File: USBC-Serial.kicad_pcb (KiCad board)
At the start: 2 copper layers, 19.5 x 25.9 mm, 10 parts, among them J1 USB_C_Receptacle_USB2.0_16P, J2 Conn_01x06_Pin, U1 CH343P

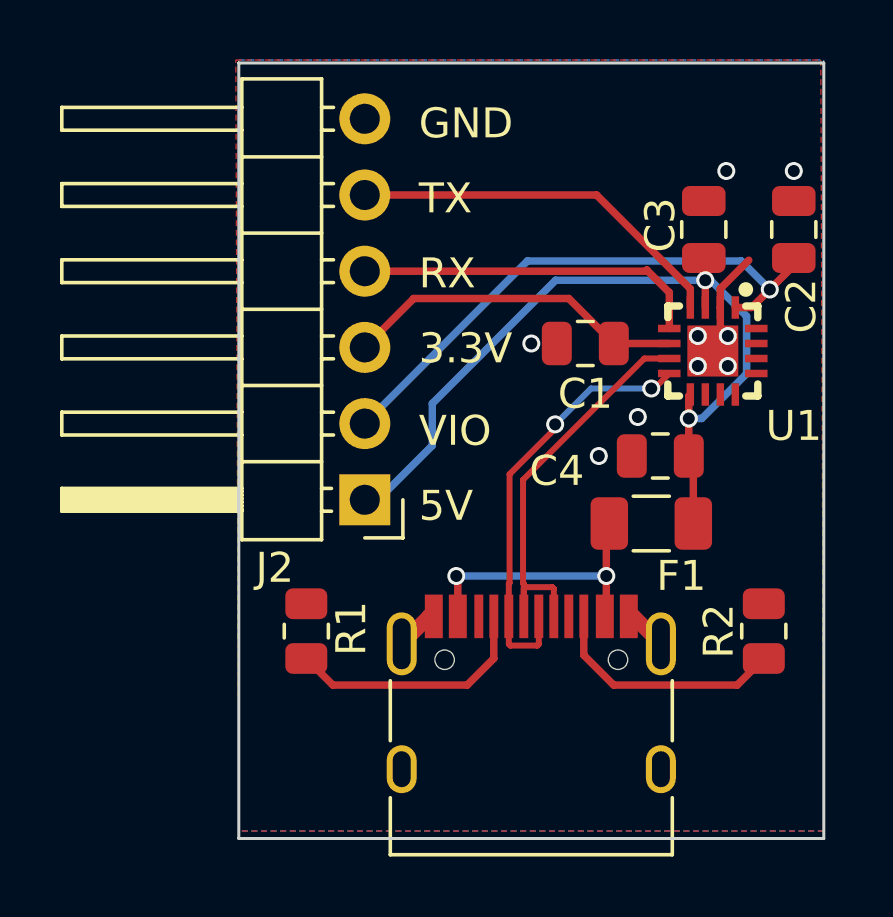
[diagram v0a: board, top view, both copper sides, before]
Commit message: fix bypass caps
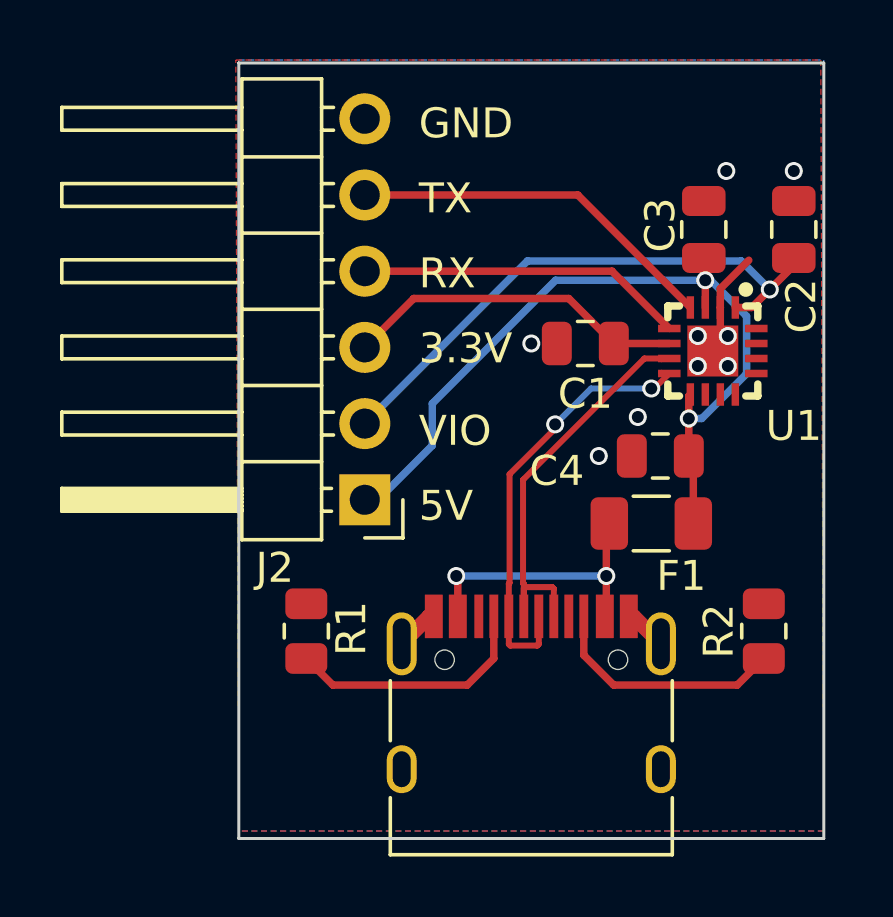
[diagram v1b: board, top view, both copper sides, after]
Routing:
- net /RXD: track 11.7 -> 10.9 mm
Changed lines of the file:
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@@
   (segment (start 25.495051 37.135483) (end 24.5 36.140432) (width 0.25) (layer "F.Cu") (net 10))
   (segment (start 29.614517 37.135483) (end 25.495051 37.135483) (width 0.25) (layer "F.Cu") (net 10))
-  (segment (start 27.35 25.25) (end 27.35 24.05) (width 0.25) (layer "F.Cu") (net 12))
-  (segment (start 26.56 23.34) (end 17.2 23.34) (width 0.25) (layer "F.Cu") (net 12))
-  (segment (start 27.35 24.05) (end 26.6 23.3) (width 0.25) (layer "F.Cu") (net 12))
-  (segment (start 26.6 23.3) (end 26.56 23.34) (width 0.25) (layer "F.Cu") (net 12))
-  (segment (start 28.05 23.925) (end 24.925 20.8) (width 0.25) (layer "F.Cu") (net 13))
-  (segment (start 24.925 20.8) (end 17.2 20.8) (width 0.25) (layer "F.Cu") (net 13))
-  (segment (start 28.05 24.55) (end 28.05 23.925) (width 0.25) (layer "F.Cu") (net 13))
+  (segment (start 25.44 23.34) (end 17.2 23.34) (width 0.25) (layer "F.Cu") (net 12))
+  (segment (start 27.35 25.25) (end 25.44 23.34) (width 0.25) (layer "F.Cu") (net 12))
+  (segment (start 28.05 24.55) (end 24.3 20.8) (width 0.25) (layer "F.Cu") (net 13))
+  (segment (start 24.3 20.8) (end 17.2 20.8) (width 0.25) (layer "F.Cu") (net 13))
   (zone (net 2) (net_name "GND") (layer "F.Cu") (hatch edge 0.5)
     (connect_pads (clearance 0.5))
